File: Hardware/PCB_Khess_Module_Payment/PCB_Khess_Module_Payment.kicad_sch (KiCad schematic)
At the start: 23 parts, among them J1 Conn_02x20_Odd_Even, J3 Conn_01x08, J4 Conn_01x04, J6 Conn_01x08

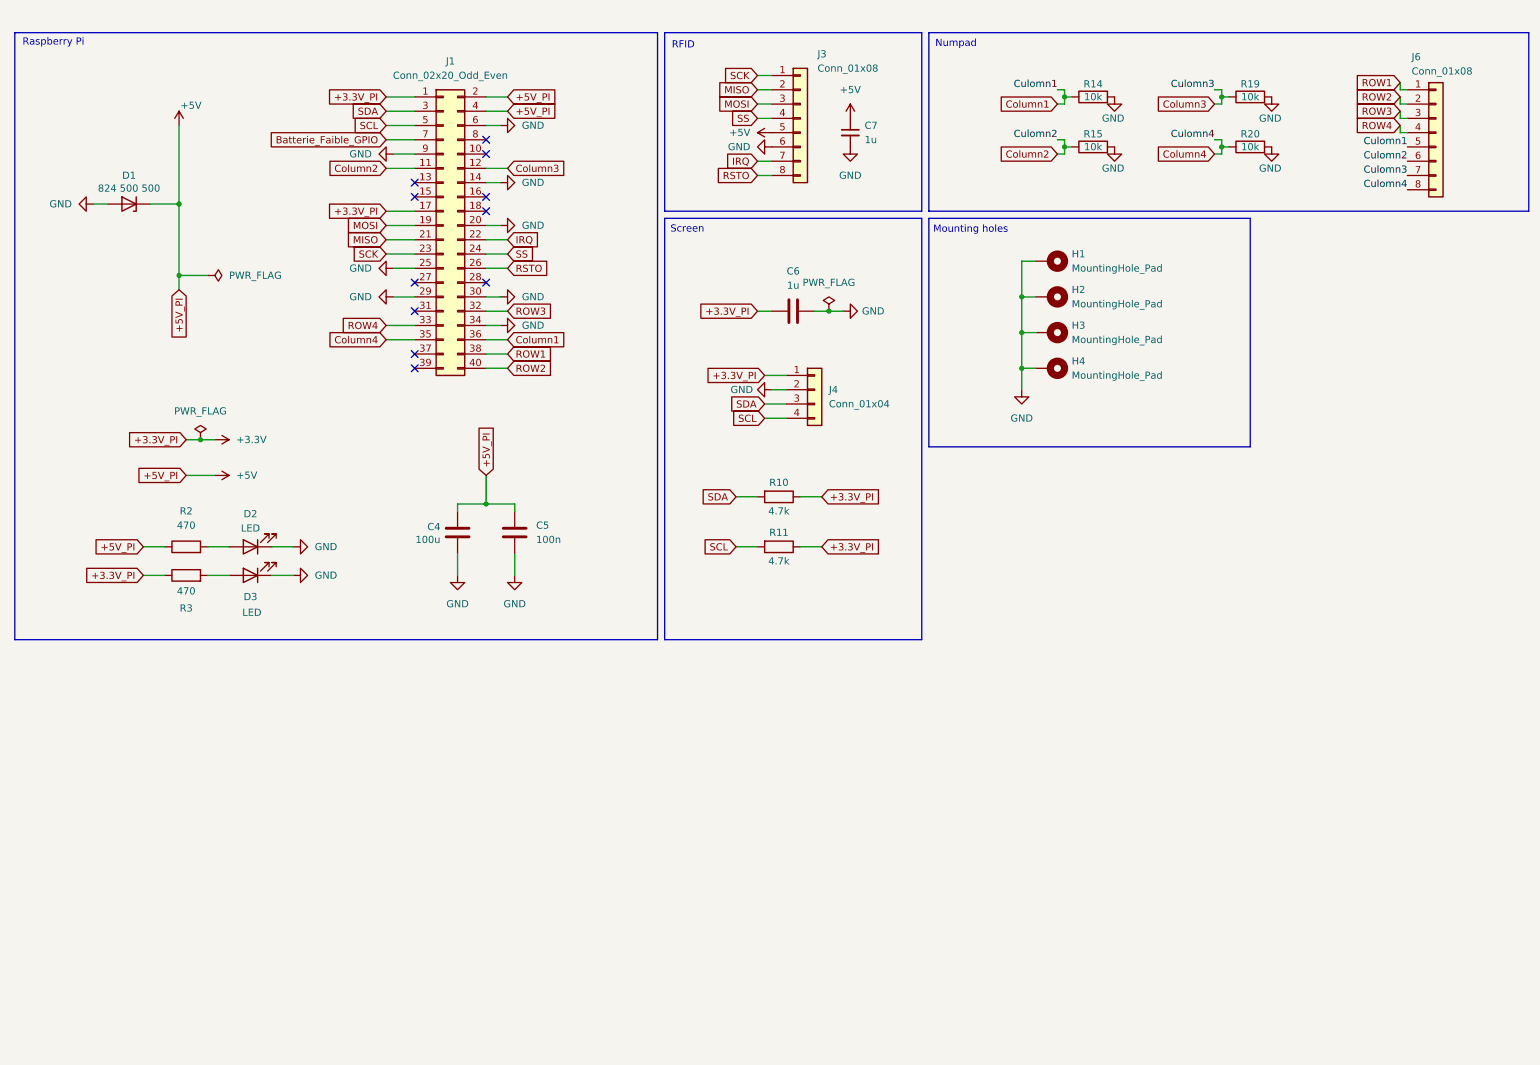
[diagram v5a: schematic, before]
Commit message: fix: update schematic
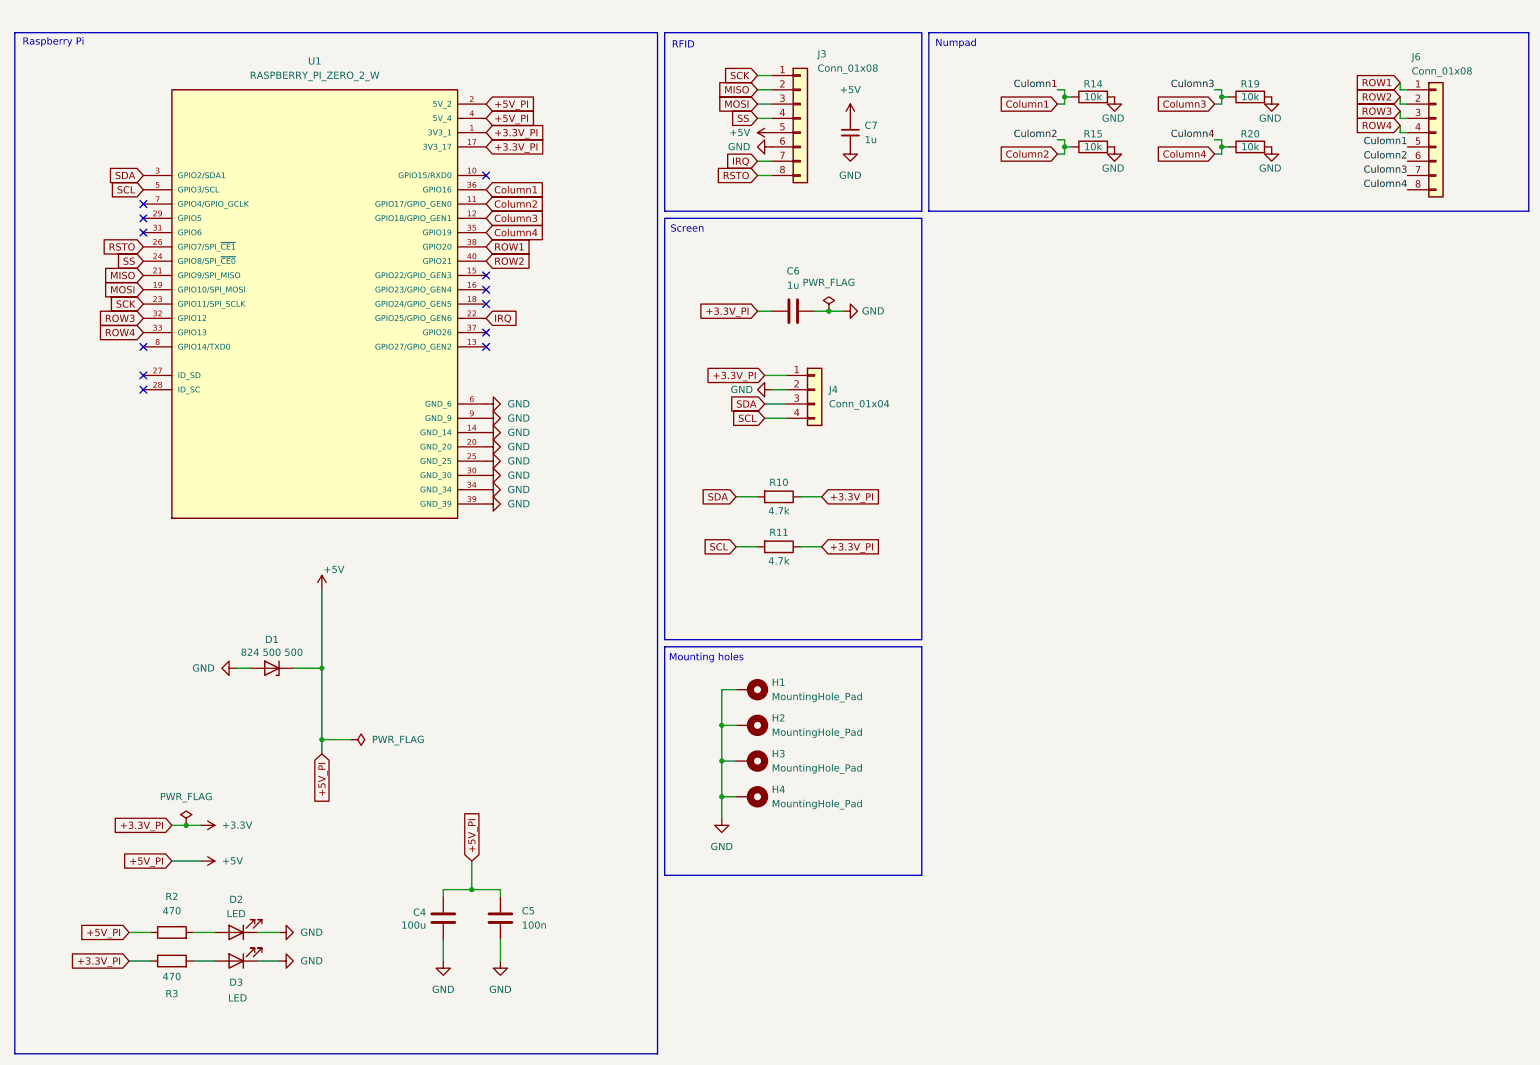
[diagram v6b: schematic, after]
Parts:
- removed J1: Conn_02x20_Odd_Even, Connector_PinHeader_1.00mm:PinHeader_2x20_P1.00mm_Vertical, symbol Connector_Generic:Conn_02x20_Odd_Even
- added U1: RASPBERRY_PI_ZERO_2_W, RASPBERRY_PI_ZERO_2_W:MODULE_RASPBERRY_PI_ZERO_2_W, symbol RASPBERRY_PI_ZERO_2_W:RASPBERRY_PI_ZERO_2_W
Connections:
- net +3.3V: now also U1.1 (3V3_1), U1.17 (3V3_17)
- net +5V: now also U1.2 (5V_2), U1.4 (5V_4)
- net Column1: now also U1.36 (GPIO16)
- net Column2: now also U1.11 (GPIO17/GPIO_GEN0)
- net Column3: now also U1.12 (GPIO18/GPIO_GEN1)
- net Column4: now also U1.35 (GPIO19)
- net GND: now also U1.14 (GND_14), U1.20 (GND_20), U1.25 (GND_25), U1.30 (GND_30), U1.34 (GND_34), U1.39 (GND_39), U1.6 (GND_6), U1.9 (GND_9)
- net IRQ: now also U1.22 (GPIO25/GPIO_GEN6)
- net MISO: now also U1.21 (GPIO9/SPI_MISO)
- net MOSI: now also U1.19 (GPIO10/SPI_MOSI)
- net ROW1: now also U1.38 (GPIO20)
- net ROW2: now also U1.40 (GPIO21)
- net ROW3: now also U1.32 (GPIO12)
- net ROW4: now also U1.33 (GPIO13)
- net RSTO: now also U1.26 (GPIO7/SPI_~{CE1})
- net SCK: now also U1.23 (GPIO11/SPI_SCLK)
- net SCL: now also U1.5 (GPIO3/SCL)
- net SDA: now also U1.3 (GPIO2/SDA1)
- net SS: now also U1.24 (GPIO8/SPI_~{CE0})
- no-connect marks 11 -> 12
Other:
- moved on the sheet: C4, C5, D1, D2, D3, H1, H2, H3, H4, R2, R3

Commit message: feat: shield pcb raspberry
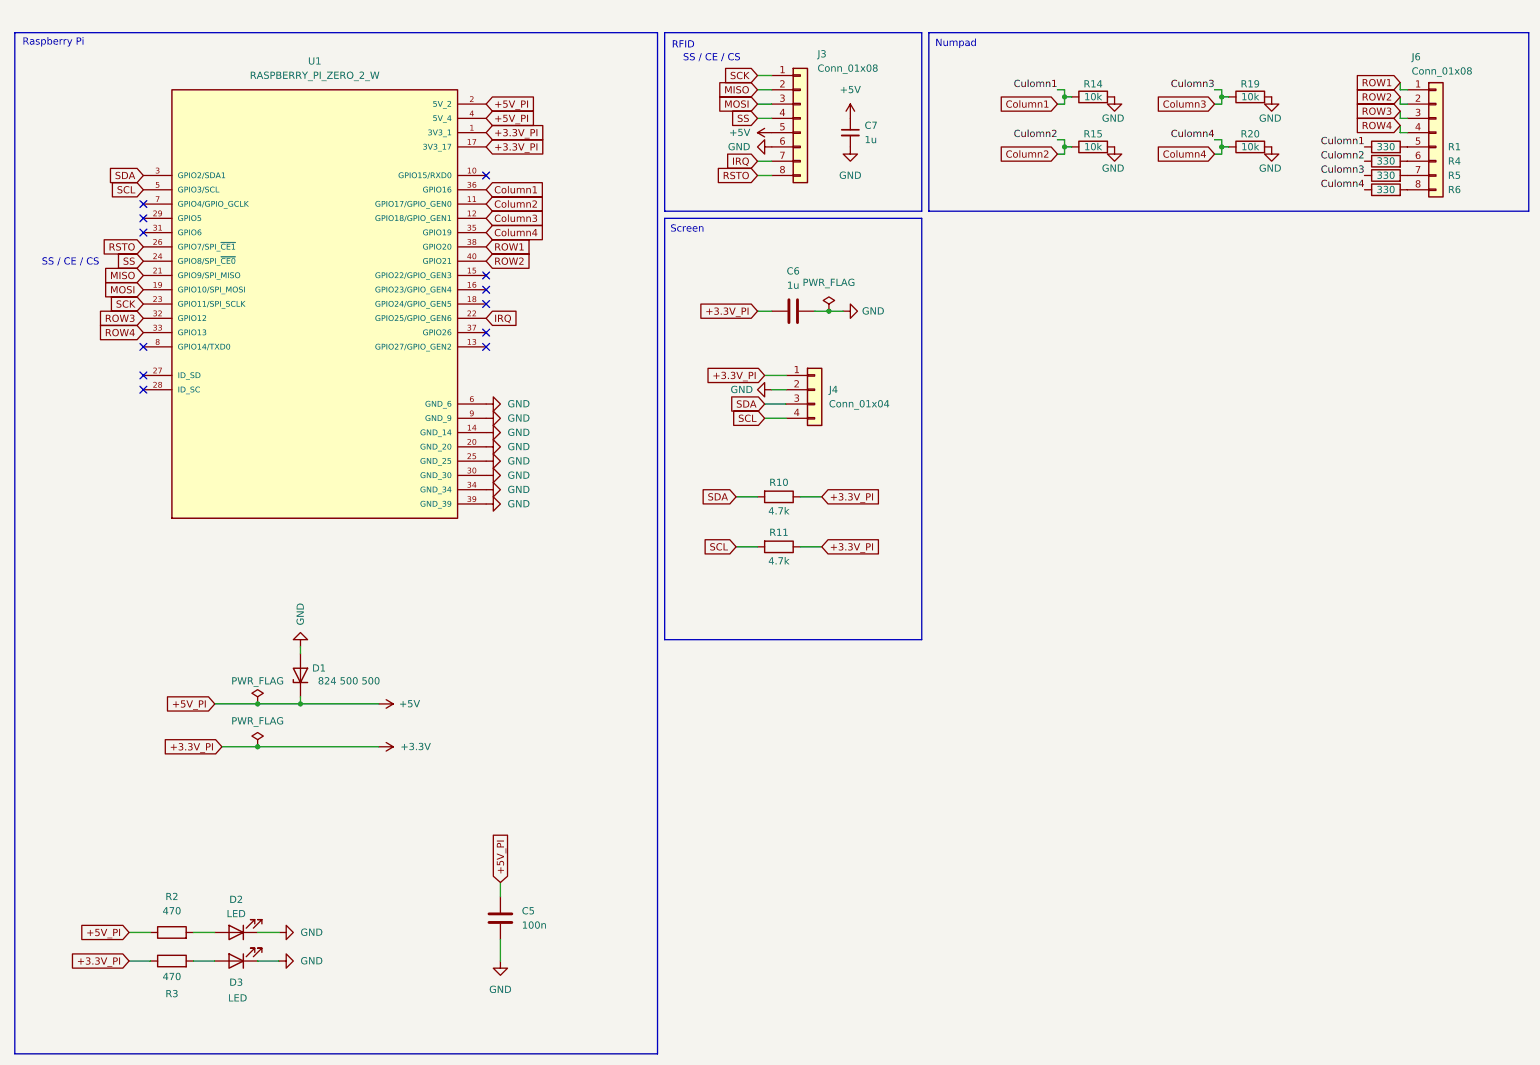
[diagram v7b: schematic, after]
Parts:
- removed C4: 100u, Capacitor_SMD:CP_Elec_6.3x7.7, symbol Device:C
- removed H1, H2, H3, H4: MountingHole_Pad, MountingHole:MountingHole_2.7mm_M2.5_Pad, symbol Mechanical:MountingHole_Pad
- added R1, R4, R5, R6: 330, Resistor_SMD:R_0402_1005Metric, symbol Device:R
- C6, C7: footprint Capacitor_SMD:CP_Elec_4x5.4 -> Capacitor_SMD:C_0603_1608Metric
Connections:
- net Column1: now also R1.1; no longer J6.5 (Pin_5)
- net Column2: now also R4.1; no longer J6.6 (Pin_6)
- net Column3: now also R5.1; no longer J6.7 (Pin_7)
- net Column4: now also R6.1; no longer J6.8 (Pin_8)
- new net: J6.7 (Pin_7), R5.2
- new net: J6.6 (Pin_6), R4.2
- new net: J6.8 (Pin_8), R6.2
- new net: J6.5 (Pin_5), R1.2
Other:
- note added: "SS / CE / CS"
- note removed: "Mounting holes"
- moved on the sheet: D1

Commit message: fix: update PCB_Khess_Module_Payment
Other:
- moved on the sheet: C5, D1, D2, D3, J6, R1, R14, R15, R19, R2, R20, R3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
